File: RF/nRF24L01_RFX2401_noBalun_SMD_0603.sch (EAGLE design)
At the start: 33 parts, among them J1 U.FL, U1 RFX2401C, U4 NRF24L01ALT1

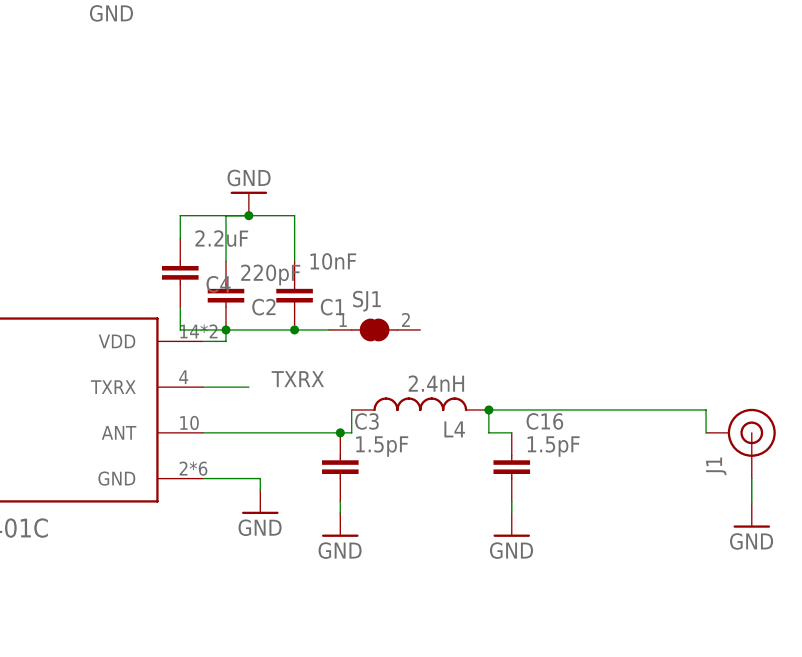
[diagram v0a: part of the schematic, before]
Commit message: Update nRF24L01_RFX2401_noBalun_SMD_0603.sch
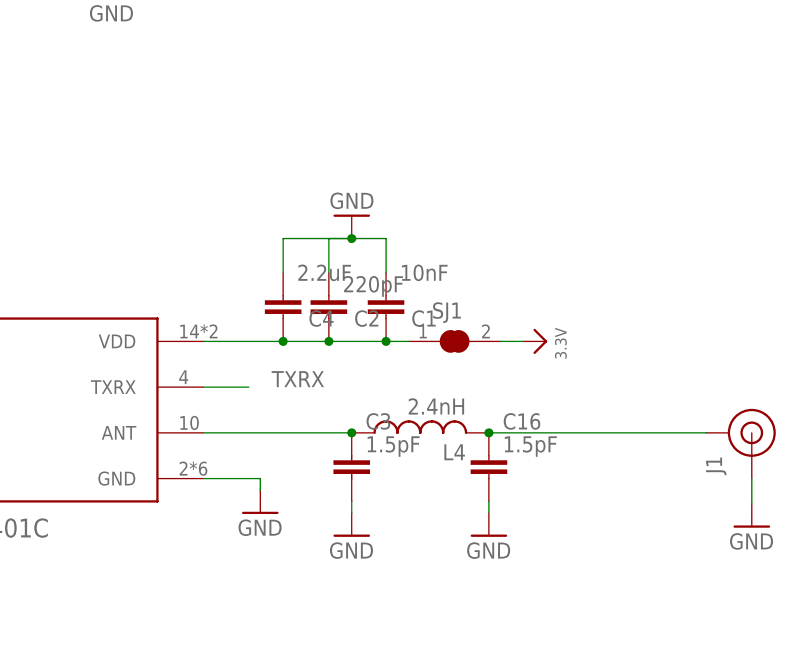
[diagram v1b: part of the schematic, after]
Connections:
- net 3.3V: now also SJ1.2
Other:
- moved on the sheet: C1, C16, C2, C3, C4, L4, SJ1
